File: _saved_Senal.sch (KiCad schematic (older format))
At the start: 19 parts, among them P1 GSG-RF-CONN, P2 GSG-RF-CONN, P3 CONN_02X04, P4 CONN_01X01, U1 AD8606, U2 ADG849, U3 AD5933

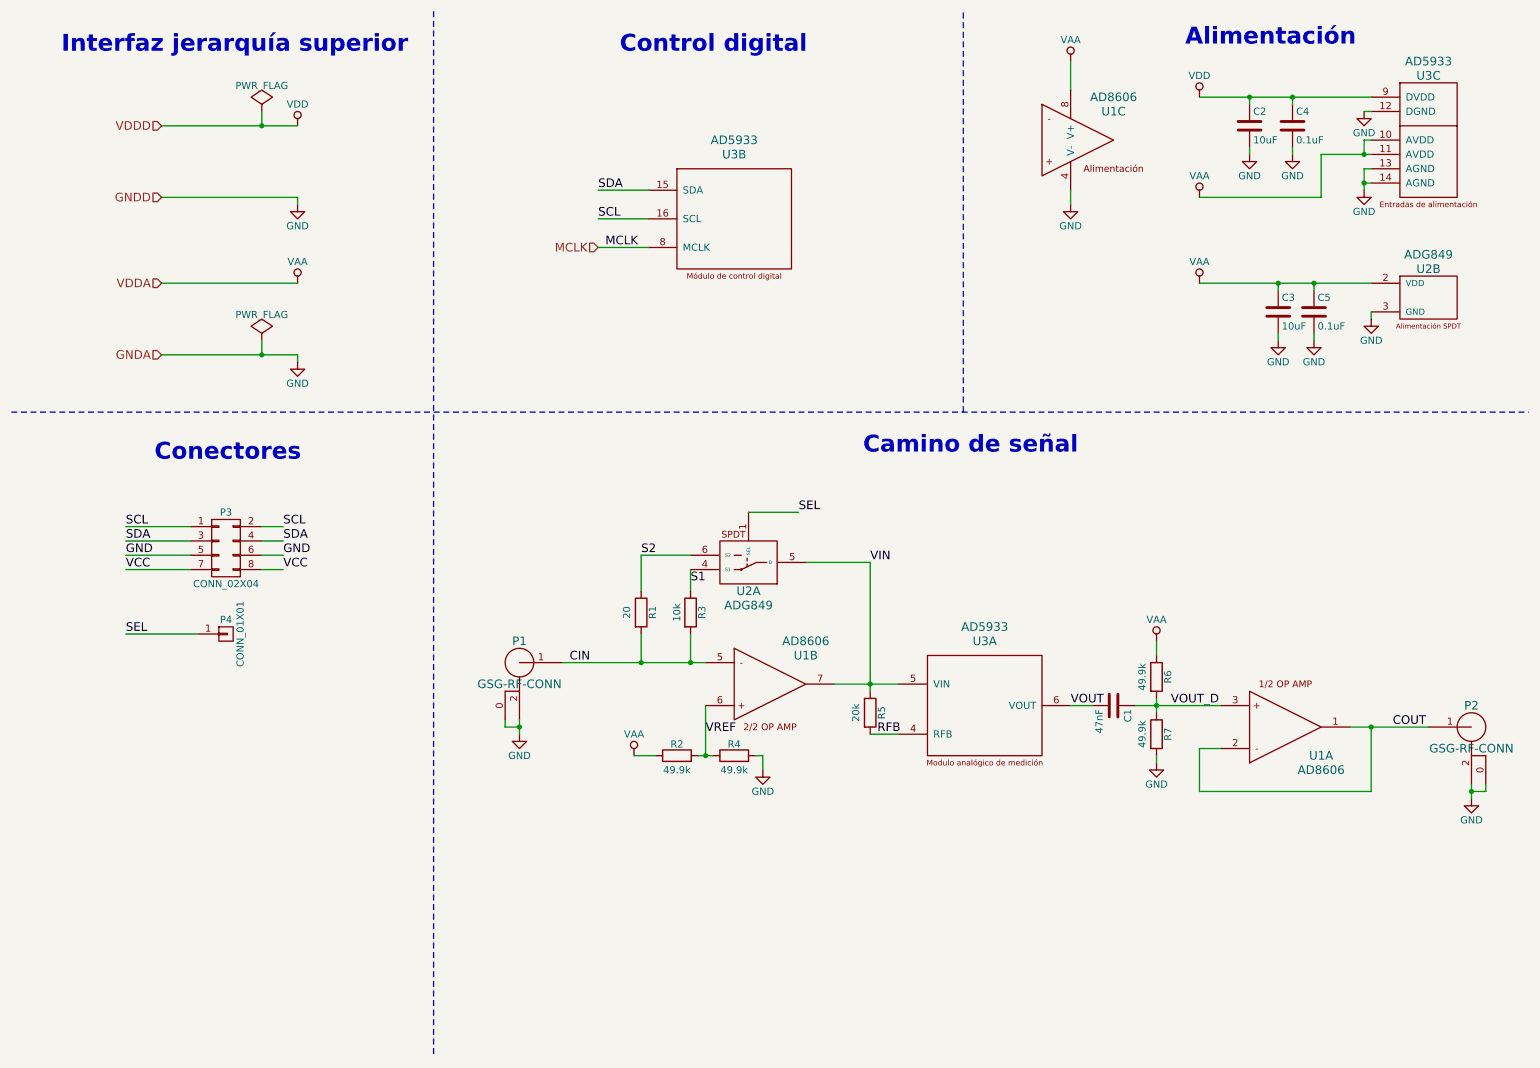
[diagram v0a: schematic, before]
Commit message: Problema de footprints solucionado
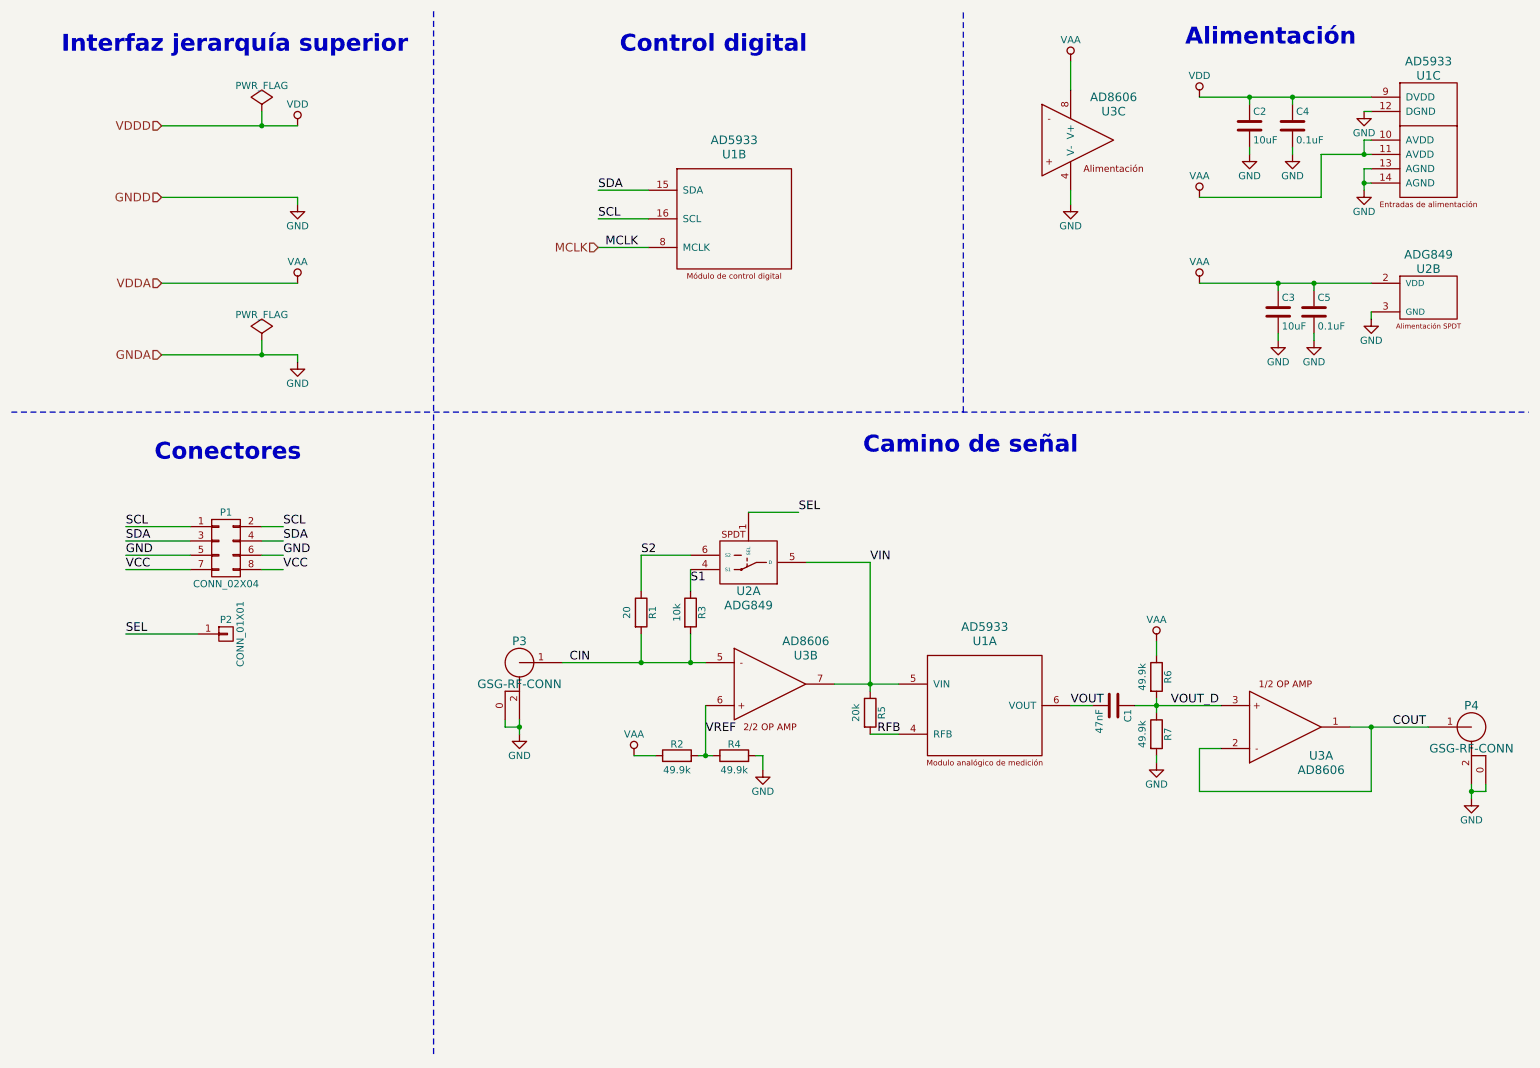
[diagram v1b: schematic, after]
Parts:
- P3: renamed from P1; footprint propios:sma -> SMA_EDGE:SMA_EDGE
- P4: renamed from P2; footprint propios:sma -> SMA_EDGE:SMA_EDGE
- renumbered P3 to P1, P4 to P2, U3 to U1, U1 to U3
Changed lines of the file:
@@
 MCLK
 $Comp
-L AD5933 U3
+L AD5933 U1
 U 3 1 582F7476
 P 10450 1400
-F 0 "U3" H 10450 1850 60  0000 C CNN
+F 0 "U1" H 10450 1850 60  0000 C CNN
 F 1 "AD5933" H 10450 1950 60  0000 C CNN
 F 2 "Housings_SSOP:SSOP-16_5.3x6.2mm_Pitch0.65mm" H 10450 1400 60  0001 C CNN
@@
 $EndComp
 $Comp
-L AD5933 U3
+L AD5933 U1
 U 2 1 582F78D1
 P 5600 1950
-F 0 "U3" H 5600 2400 60  0000 C CNN
+F 0 "U1" H 5600 2400 60  0000 C CNN
 F 1 "AD5933" H 5600 2500 60  0000 C CNN
 F 2 "Housings_SSOP:SSOP-16_5.3x6.2mm_Pitch0.65mm" H 5600 1950 60  0001 C CNN
@@
 $EndComp
 $Comp
-L AD5933 U3
+L AD5933 U1
 U 1 1 582F791E
 P 7350 5350
-F 0 "U3" H 7350 5800 60  0000 C CNN
+F 0 "U1" H 7350 5800 60  0000 C CNN
 F 1 "AD5933" H 7350 5900 60  0000 C CNN
 F 2 "Housings_SSOP:SSOP-16_5.3x6.2mm_Pitch0.65mm" H 7350 5350 60  0001 C CNN
@@
 $EndComp
 $Comp
-L AD8606 U1
+L AD8606 U3
 U 3 1 582F7A24
 P 8000 1400
-F 0 "U1" H 8250 1600 60  0000 C CNN
+F 0 "U3" H 8250 1600 60  0000 C CNN
 F 1 "AD8606" H 8250 1700 60  0000 C CNN
 F 2 "Housings_SSOP:MSOP-8_3x3mm_Pitch0.65mm" H 8000 1400 60  0001 C CNN
@@
 $EndComp
 $Comp
-L AD8606 U1
+L AD8606 U3
 U 1 1 582F8028
 P 9450 5500
-F 0 "U1" H 9700 5700 60  0000 C CNN
+F 0 "U3" H 9700 5700 60  0000 C CNN
 F 1 "AD8606" H 9700 5800 60  0000 C CNN
 F 2 "Housings_SSOP:MSOP-8_3x3mm_Pitch0.65mm" H 9450 5500 60  0001 C CNN
@@
 $EndComp
 $Comp
-L AD8606 U1
+L AD8606 U3
 U 2 1 582F8067
 P 5850 5200
-F 0 "U1" H 6100 5400 60  0000 C CNN
+F 0 "U3" H 6100 5400 60  0000 C CNN
 F 1 "AD8606" H 6100 5500 60  0000 C CNN
 F 2 "Housings_SSOP:MSOP-8_3x3mm_Pitch0.65mm" H 5850 5200 60  0001 C CNN
@@
 $EndComp
 $Comp
-L GSG-RF-CONN P2
+L GSG-RF-CONN P4
 U 1 1 582FC1E0
 P 10750 5500
-F 0 "P2" H 10750 5650 60  0000 C CNN
+F 0 "P4" H 10750 5650 60  0000 C CNN
 F 1 "GSG-RF-CONN" H 10750 5350 60  0000 C CNN
-F 2 "propios:sma" H 10750 5500 60  0001 C CNN
+F 2 "SMA_EDGE:SMA_EDGE" H 10750 5500 60  0001 C CNN
 F 3 "" H 10750 5500 60  0000 C CNN
 F 4 "WM5534-ND" H 10750 5500 60  0001 C CNN "Digikey#"
@@
 $EndComp
 $Comp
-L GSG-RF-CONN P1
+L GSG-RF-CONN P3
 U 1 1 582FCD4C
 P 4100 5050
-F 0 "P1" H 4100 5200 60  0000 C CNN
+F 0 "P3" H 4100 5200 60  0000 C CNN
 F 1 "GSG-RF-CONN" H 4100 4900 60  0000 C CNN
-F 2 "propios:sma" H 4100 5050 60  0001 C CNN
+F 2 "SMA_EDGE:SMA_EDGE" H 4100 5050 60  0001 C CNN
 F 3 "" H 4100 5050 60  0000 C CNN
 	1    4100 5050
@@
 Camino de señal
 $Comp
-L CONN_02X04 P3
+L CONN_02X04 P1
 U 1 1 58375283
 P 2050 4250
-F 0 "P3" H 2050 4500 50  0000 C CNN
+F 0 "P1" H 2050 4500 50  0000 C CNN
 F 1 "CONN_02X04" H 2050 4000 50  0000 C CNN
 F 2 "Pin_Headers:Pin_Header_Straight_2x04" H 2050 3050 50  0001 C CNN
@@
 VCC
 $Comp
-L CONN_01X01 P4
+L CONN_01X01 P2
 U 1 1 5837592F
 P 2050 4850
-F 0 "P4" H 2050 4950 50  0000 C CNN
+F 0 "P2" H 2050 4950 50  0000 C CNN
 F 1 "CONN_01X01" V 2150 4850 50  0000 C CNN
 F 2 "Pin_Headers:Pin_Header_Straight_1x01" H 2050 4850 50  0001 C CNN
